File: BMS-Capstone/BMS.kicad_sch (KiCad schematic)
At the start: 0 parts

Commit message: Finished teensy
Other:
- added sheet Monitoring (Monitoring.kicad_sch)
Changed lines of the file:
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@@
+	)
+	(sheet
+		(at 67.31 100.33)
+		(size 40.64 31.75)
+		(exclude_from_sim no)
+		(in_bom yes)
+		(on_board yes)
+		(dnp no)
+		(fields_autoplaced yes)
+		(stroke
+			(width 0.1524)
+			(type solid)
+		)
+		(fill
+			(color 0 0 0 0.0000)
+		)
+		(property "Sheetname" "Monitoring"
+			(at 67.31 99.6184 0)
+			(effects
+				(font
+					(size 1.27 1.27)
+				)
+				(justify left bottom)
+			)
+		)
+		(property "Sheetfile" "Monitoring.kicad_sch"
+			(at 67.31 132.6646 0)
+			(effects
+				(font
+					(size 1.27 1.27)
+				)
+				(justify left top)
+			)
+		)
+		(instances
+			(project "BMS"
+				(path "/f2da9442-ca05-4687-a880-d5cd24c39f1d"
+					(page "5")
+				)
+			)
+		)
 	)
 	(sheet

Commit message: im stupid
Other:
- note added: "DELETE BEFORE YOU MERGE IDIOT"
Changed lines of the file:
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@@
 	(generator_version "9.0")
 	(paper "A4")
+	(rectangle
+		(start 48.26 93.98)
+		(end 128.27 144.78)
+		(stroke
+			(width 0)
+			(type default)
+		)
+		(fill
+			(type none)
+		)
+	)
+	(text "DELETE BEFORE YOU MERGE IDIOT"
+		(exclude_from_sim no)
+		(at 87.884 139.7 0)
+		(effects
+			(font
+				(size 2.54 2.54)
+			)
+		)
+	)
 	(sheet
 		(at 161.29 44.45)

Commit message: did a thing
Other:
- note removed: "DELETE BEFORE YOU MERGE IDIOT"
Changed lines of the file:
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@@
 	(generator_version "9.0")
 	(paper "A4")
-	(rectangle
-		(start 48.26 93.98)
-		(end 128.27 144.78)
-		(stroke
-			(width 0)
-			(type default)
-		)
-		(fill
-			(type none)
-		)
-	)
-	(text "DELETE BEFORE YOU MERGE IDIOT"
-		(exclude_from_sim no)
-		(at 87.884 139.7 0)
-		(effects
-			(font
-				(size 2.54 2.54)
-			)
-		)
-	)
 	(sheet
 		(at 161.29 44.45)

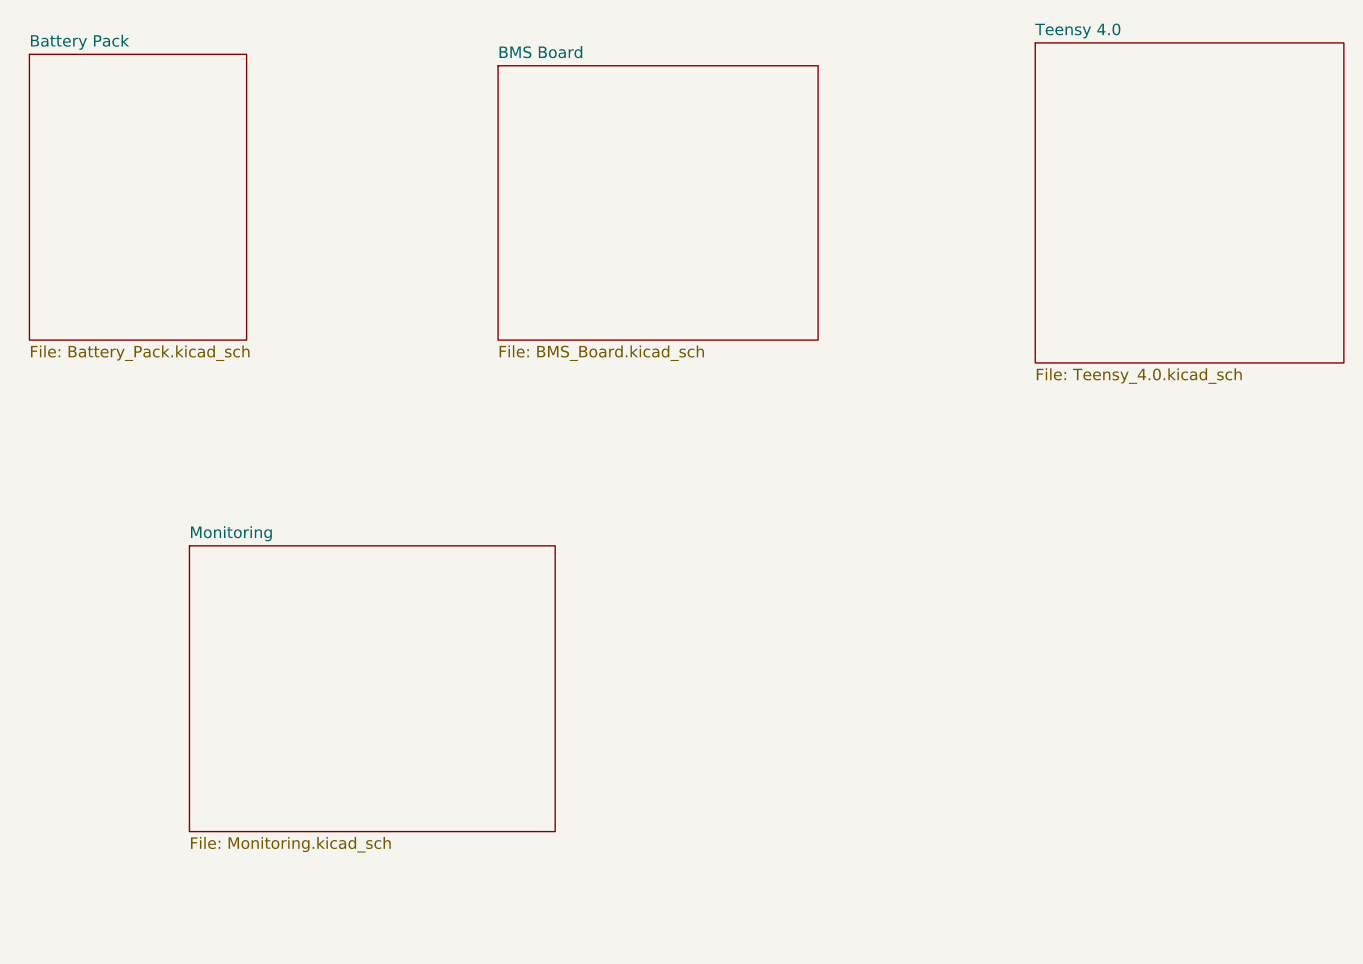
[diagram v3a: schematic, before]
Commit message: Added main Schematic to branch and linked components to PCB
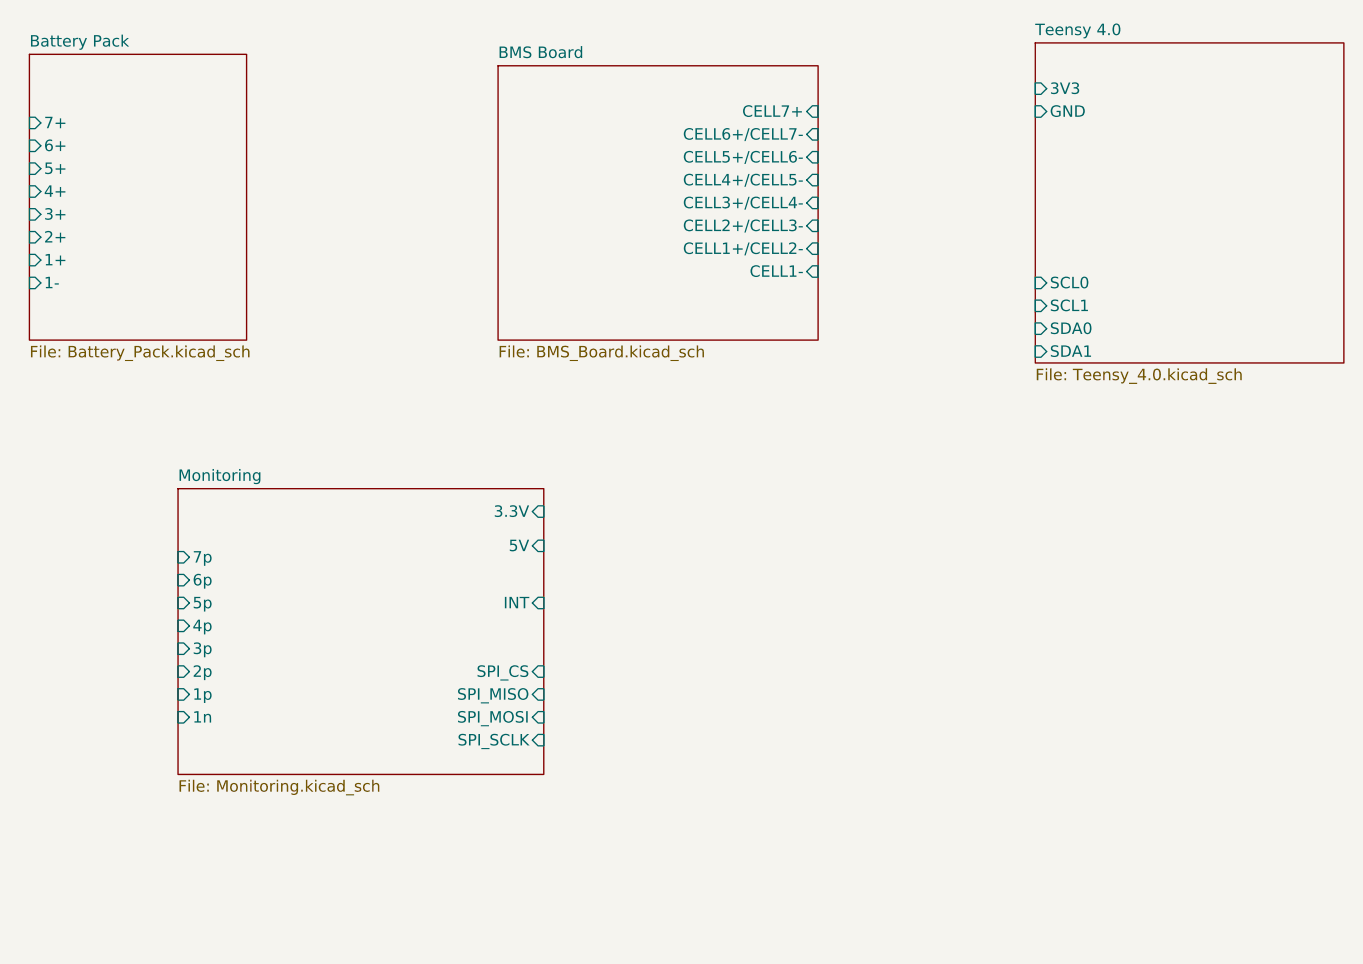
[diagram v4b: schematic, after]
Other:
- sheet BMS Board ports: added CELL1+/CELL2-, CELL1-, CELL2+/CELL3-, CELL3+/CELL4-, CELL4+/CELL5-, CELL5+/CELL6-, CELL6+/CELL7-, CELL7+; removed none
- sheet Battery Pack ports: added 1+, 1-, 2+, 3+, 4+, 5+, 6+, 7+; removed none
- sheet Monitoring ports: added 1n, 1p, 2p, 3.3V, 3p, 4p, 5V, 5p, 6p, 7p, INT, SPI_CS, SPI_MISO, SPI_MOSI, SPI_SCLK; removed none
- sheet Teensy 4.0 ports: added 3V3, GND, SCL0, SCL1, SDA0, SDA1; removed none

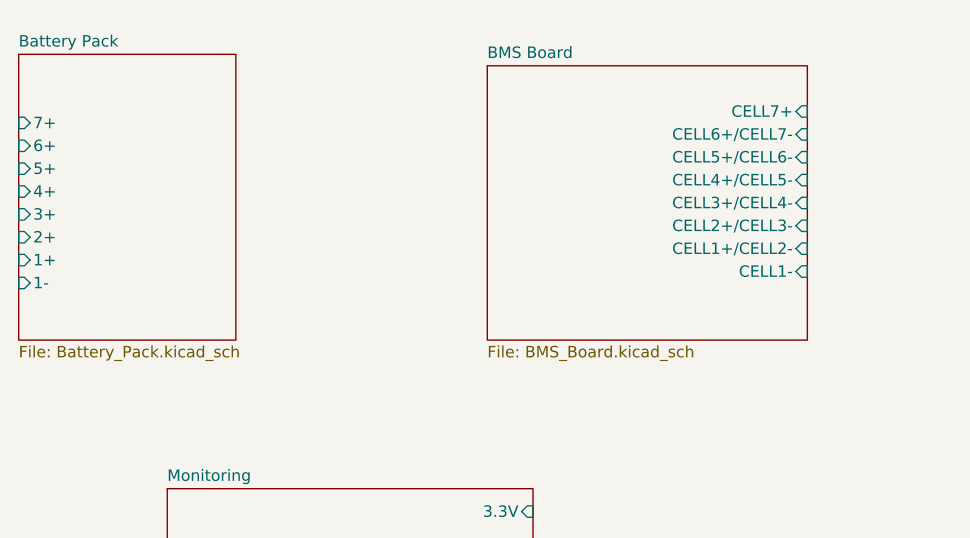
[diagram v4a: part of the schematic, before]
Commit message: Added connector to balancing schematic
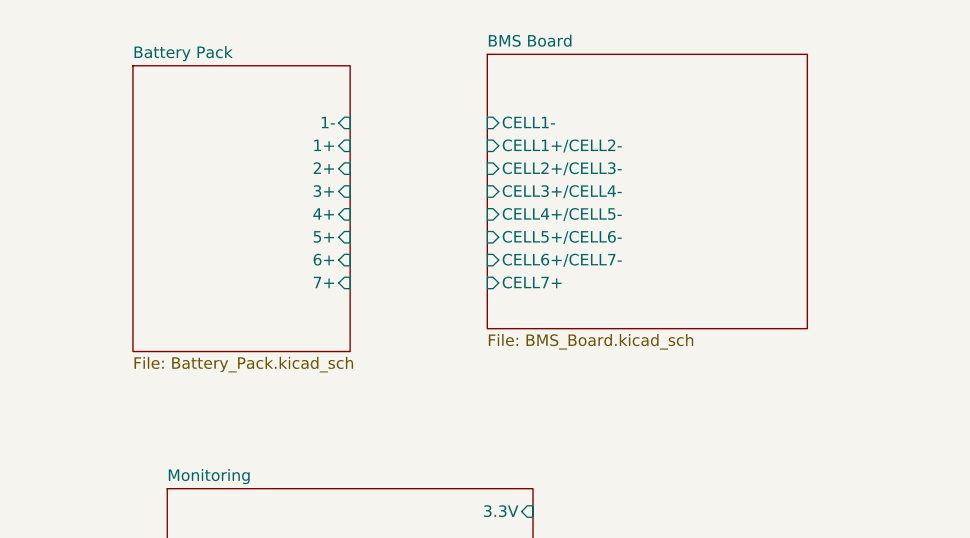
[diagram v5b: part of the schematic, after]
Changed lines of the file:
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@@
 	)
 	(sheet
-		(at 101.6 46.99)
+		(at 101.6 45.72)
 		(size 35.56 30.48)
 		(exclude_from_sim no)
@@
 		)
 		(property "Sheetname" "BMS Board"
-			(at 101.6 46.2784 0)
+			(at 101.6 45.0084 0)
 			(effects
 				(font
@@
 		)
 		(property "Sheetfile" "BMS_Board.kicad_sch"
-			(at 101.6 78.0546 0)
+			(at 101.6 76.7846 0)
 			(effects
 				(font
@@
 		)
 		(pin "CELL1+{slash}CELL2-" input
-			(at 137.16 67.31 0)
-			(effects
-				(font
-					(size 1.27 1.27)
-				)
-				(justify right)
+			(at 101.6 55.88 180)
+			(effects
+				(font
+					(size 1.27 1.27)
+				)
+				(justify left)
 			)
 		)
 		(pin "CELL1-" input
-			(at 137.16 69.85 0)
-			(effects
-				(font
-					(size 1.27 1.27)
-				)
-				(justify right)
+			(at 101.6 53.34 180)
+			(effects
+				(font
+					(size 1.27 1.27)
+				)
+				(justify left)
 			)
 		)
 		(pin "CELL2+{slash}CELL3-" input
-			(at 137.16 64.77 0)
-			(effects
-				(font
-					(size 1.27 1.27)
-				)
-				(justify right)
+			(at 101.6 58.42 180)
+			(effects
+				(font
+					(size 1.27 1.27)
+				)
+				(justify left)
 			)
 		)
 		(pin "CELL3+{slash}CELL4-" input
-			(at 137.16 62.23 0)
-			(effects
-				(font
-					(size 1.27 1.27)
-				)
-				(justify right)
+			(at 101.6 60.96 180)
+			(effects
+				(font
+					(size 1.27 1.27)
+				)
+				(justify left)
 			)
 		)
 		(pin "CELL4+{slash}CELL5-" input
-			(at 137.16 59.69 0)
-			(effects
-				(font
-					(size 1.27 1.27)
-				)
-				(justify right)
+			(at 101.6 63.5 180)
+			(effects
+				(font
+					(size 1.27 1.27)
+				)
+				(justify left)
 			)
 		)
 		(pin "CELL5+{slash}CELL6-" input
-			(at 137.16 57.15 0)
-			(effects
-				(font
-					(size 1.27 1.27)
-				)
-				(justify right)
+			(at 101.6 66.04 180)
+			(effects
+				(font
+					(size 1.27 1.27)
+				)
+				(justify left)
 			)
 		)
 		(pin "CELL6+{slash}CELL7-" input
-			(at 137.16 54.61 0)
-			(effects
-				(font
-					(size 1.27 1.27)
-				)
-				(justify right)
+			(at 101.6 68.58 180)
+			(effects
+				(font
+					(size 1.27 1.27)
+				)
+				(justify left)
 			)
 		)
 		(pin "CELL7+" input
-			(at 137.16 52.07 0)
-			(effects
-				(font
-					(size 1.27 1.27)
-				)
-				(justify right)
+			(at 101.6 71.12 180)
+			(effects
+				(font
+					(size 1.27 1.27)
+				)
+				(justify left)
 			)
 		)
@@
 	)
 	(sheet
-		(at 49.53 45.72)
+		(at 62.23 46.99)
 		(size 24.13 31.75)
 		(exclude_from_sim no)
@@
 		)
 		(property "Sheetname" "Battery Pack"
-			(at 49.53 45.0084 0)
+			(at 62.23 46.2784 0)
 			(effects
 				(font
@@
 		)
 		(property "Sheetfile" "Battery_Pack.kicad_sch"
-			(at 49.53 78.0546 0)
+			(at 62.23 79.3246 0)
 			(effects
 				(font
@@
 		)
 		(pin "1+" input
-			(at 49.53 68.58 180)
-			(effects
-				(font
-					(size 1.27 1.27)
-				)
-				(justify left)
+			(at 86.36 55.88 0)
+			(effects
+				(font
+					(size 1.27 1.27)
+				)
+				(justify right)
 			)
 		)
 		(pin "2+" input
-			(at 49.53 66.04 180)
-			(effects
-				(font
-					(size 1.27 1.27)
-				)
-				(justify left)
+			(at 86.36 58.42 0)
+			(effects
+				(font
+					(size 1.27 1.27)
+				)
+				(justify right)
 			)
 		)
 		(pin "3+" input
-			(at 49.53 63.5 180)
-			(effects
-				(font
-					(size 1.27 1.27)
-				)
-				(justify left)
+			(at 86.36 60.96 0)
+			(effects
+				(font
+					(size 1.27 1.27)
+				)
+				(justify right)
 			)
 		)
 		(pin "4+" input
-			(at 49.53 60.96 180)
-			(effects
-				(font
-					(size 1.27 1.27)
-				)
-				(justify left)
+			(at 86.36 63.5 0)
+			(effects
+				(font
+					(size 1.27 1.27)
+				)
+				(justify right)
 			)
 		)
 		(pin "5+" input
-			(at 49.53 58.42 180)
-			(effects
-				(font
-					(size 1.27 1.27)
-				)
-				(justify left)
+			(at 86.36 66.04 0)
+			(effects
+				(font
+					(size 1.27 1.27)
+				)
+				(justify right)
 			)
 		)
 		(pin "6+" input
-			(at 49.53 55.88 180)
-			(effects
-				(font
-					(size 1.27 1.27)
-				)
-				(justify left)
+			(at 86.36 68.58 0)
+			(effects
+				(font
+					(size 1.27 1.27)
+				)
+				(justify right)
 			)
 		)
 		(pin "7+" input
-			(at 49.53 53.34 180)
-			(effects
-				(font
-					(size 1.27 1.27)
-				)
-				(justify left)
+			(at 86.36 71.12 0)
+			(effects
+				(font
+					(size 1.27 1.27)
+				)
+				(justify right)
 			)
 		)
 		(pin "1-" input
-			(at 49.53 71.12 180)
-			(effects
-				(font
-					(size 1.27 1.27)
-				)
-				(justify left)
-			)
-		)
+			(at 86.36 53.34 0)
+			(effects
+				(font
+					(size 1.27 1.27)
+				)
+				(justify right)
+			)
+		)
